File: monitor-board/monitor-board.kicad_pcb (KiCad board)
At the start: 2 copper layers, 55.9 x 53.3 mm, 26 parts, among them J1 Conn_01x06, SW1 SW_IO12, SW2 SW_IO13, SW3 SW_IO14, SW4 SW_IO15, SW5 SW_IO32, SW6 SW_IO33, SW7 SW_IO34, SW8 SW_IO35, U1 ESP32-WROOM-32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

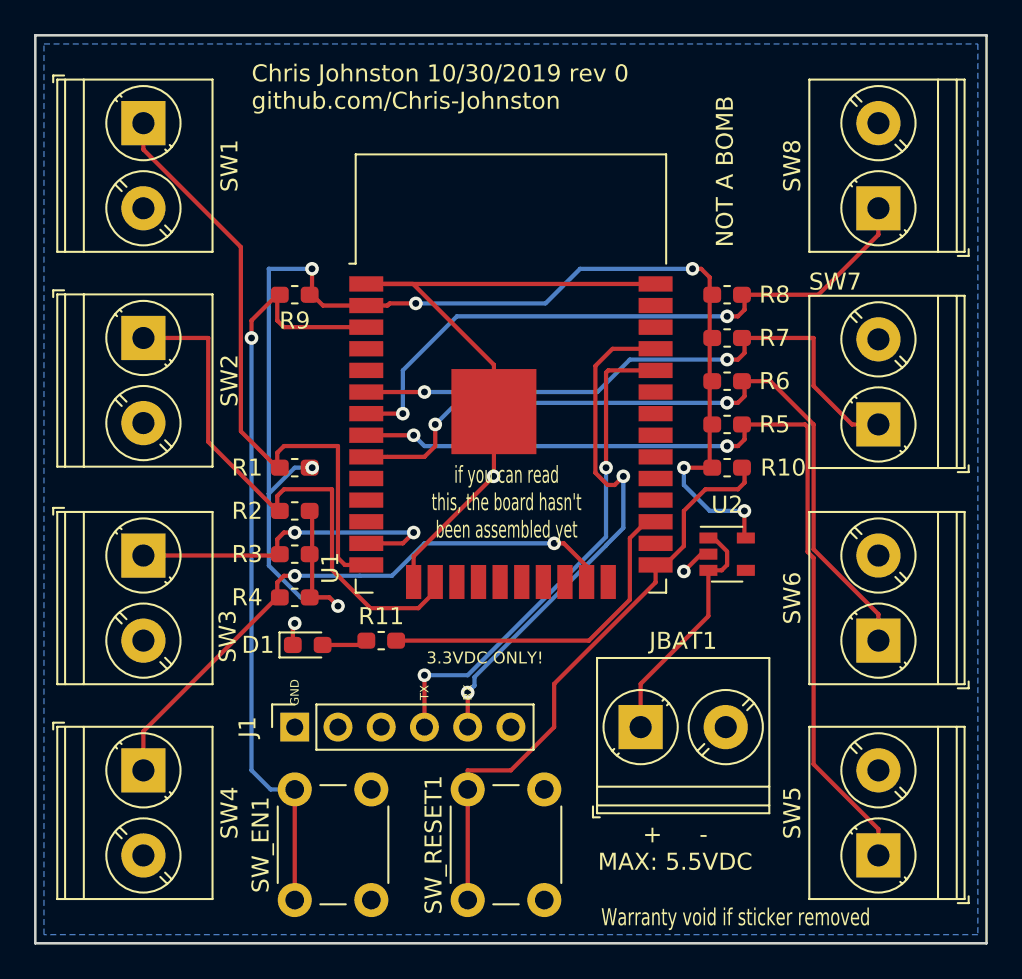
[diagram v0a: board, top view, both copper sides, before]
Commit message: trim edges of board
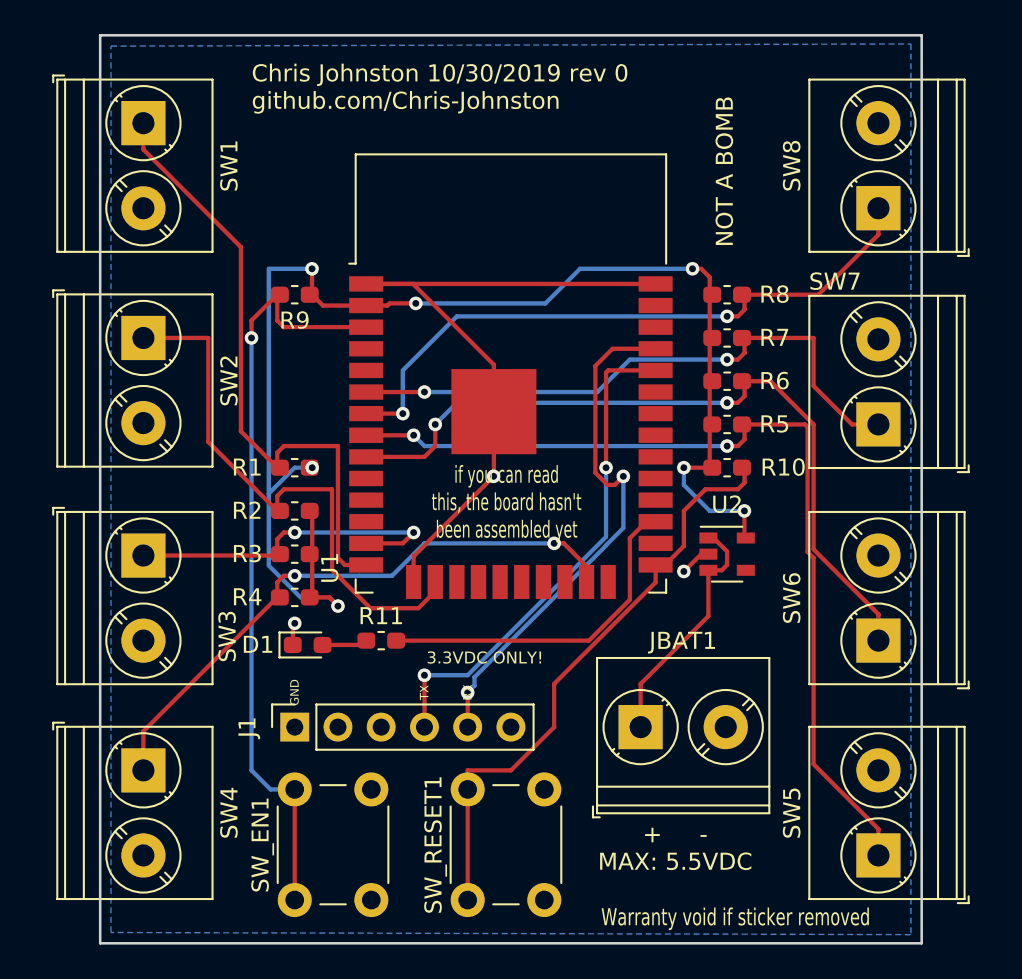
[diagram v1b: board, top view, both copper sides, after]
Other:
- board size 55.9 x 53.3 mm -> 48.3 x 53.3 mm
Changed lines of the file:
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@@
     (effects (font (size 1 1) (thickness 0.15)))
   )
-  (gr_line (start 81.28 25.4) (end 25.4 25.4) (layer Edge.Cuts) (width 0.15))
-  (gr_line (start 81.28 78.74) (end 81.28 25.4) (layer Edge.Cuts) (width 0.15))
-  (gr_line (start 25.4 78.74) (end 81.28 78.74) (layer Edge.Cuts) (width 0.15))
-  (gr_line (start 25.4 25.4) (end 25.4 78.74) (layer Edge.Cuts) (width 0.15))
+  (gr_line (start 77.47 25.4) (end 29.21 25.4) (layer Edge.Cuts) (width 0.15))
+  (gr_line (start 77.47 78.74) (end 77.47 25.4) (layer Edge.Cuts) (width 0.15))
+  (gr_line (start 29.21 78.74) (end 77.47 78.74) (layer Edge.Cuts) (width 0.15))
+  (gr_line (start 29.21 25.4) (end 29.21 78.74) (layer Edge.Cuts) (width 0.15))
   (via (at 52.324 51.308) (size 0.8) (drill 0.4) (layers F.Cu B.Cu) (net 1))
   (segment (start 52.34 47.505) (end 52.34 51.292) (width 0.25) (layer F.Cu) (net 1))
@@
     (polygon
       (pts
-        (xy 25.908 25.908) (xy 80.772 25.908) (xy 80.772 78.232) (xy 25.908 78.232)
+        (xy 29.845 26.035) (xy 76.835 25.908) (xy 76.835 78.232) (xy 29.845 78.105)
       )
     )
